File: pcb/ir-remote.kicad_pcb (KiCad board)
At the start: 2 copper layers, 127.9 x 53.5 mm, 104 parts, among them J1 Conn_01x02, J12 Conn_01x04, J2 Conn_01x02, J3 Pins_02x04_P2.54mm_SMT, J4 USB-C_Receptacle_Molex_217179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, J5 Jack_RCA_Stereo, J6 Conn_01x03, J7 Jack_RCA_Stereo, J8 Conn_01x02, U1 STM32G431CBTx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

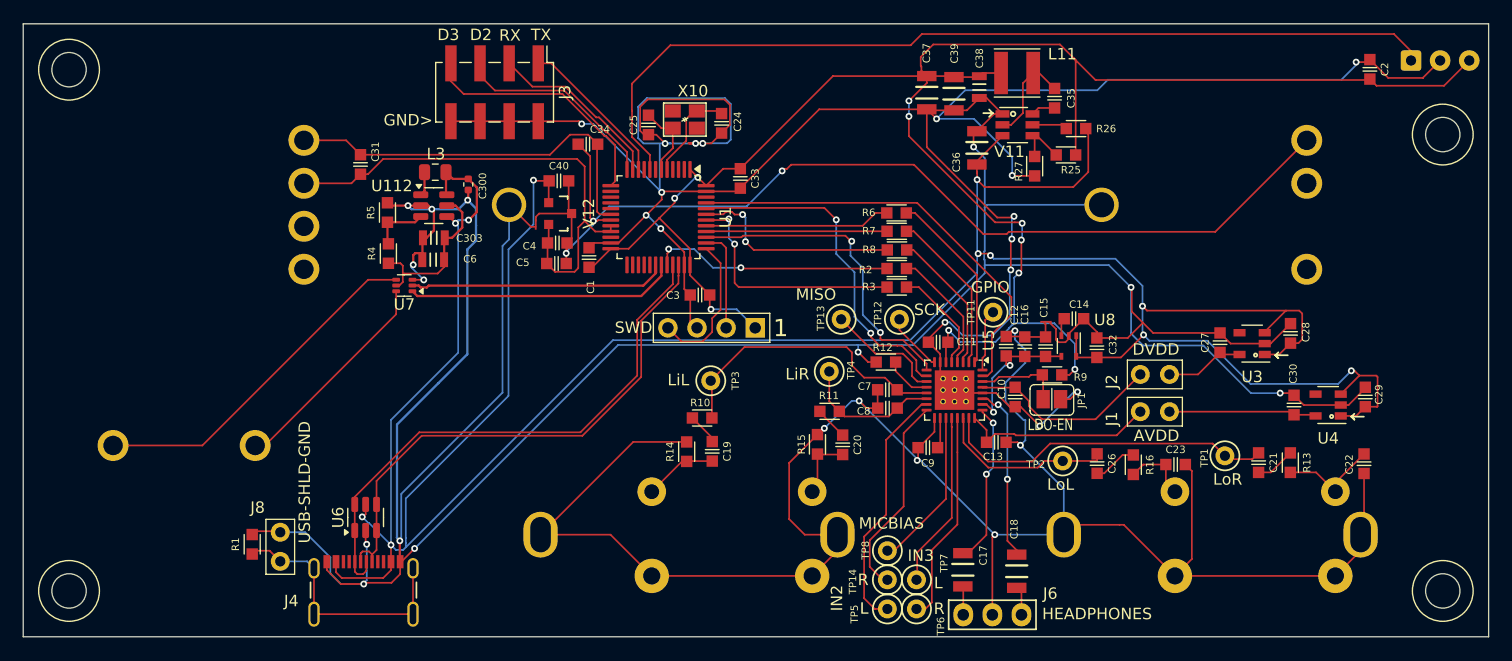
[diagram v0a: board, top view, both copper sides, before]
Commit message: Enclosure and PCB matched and fit
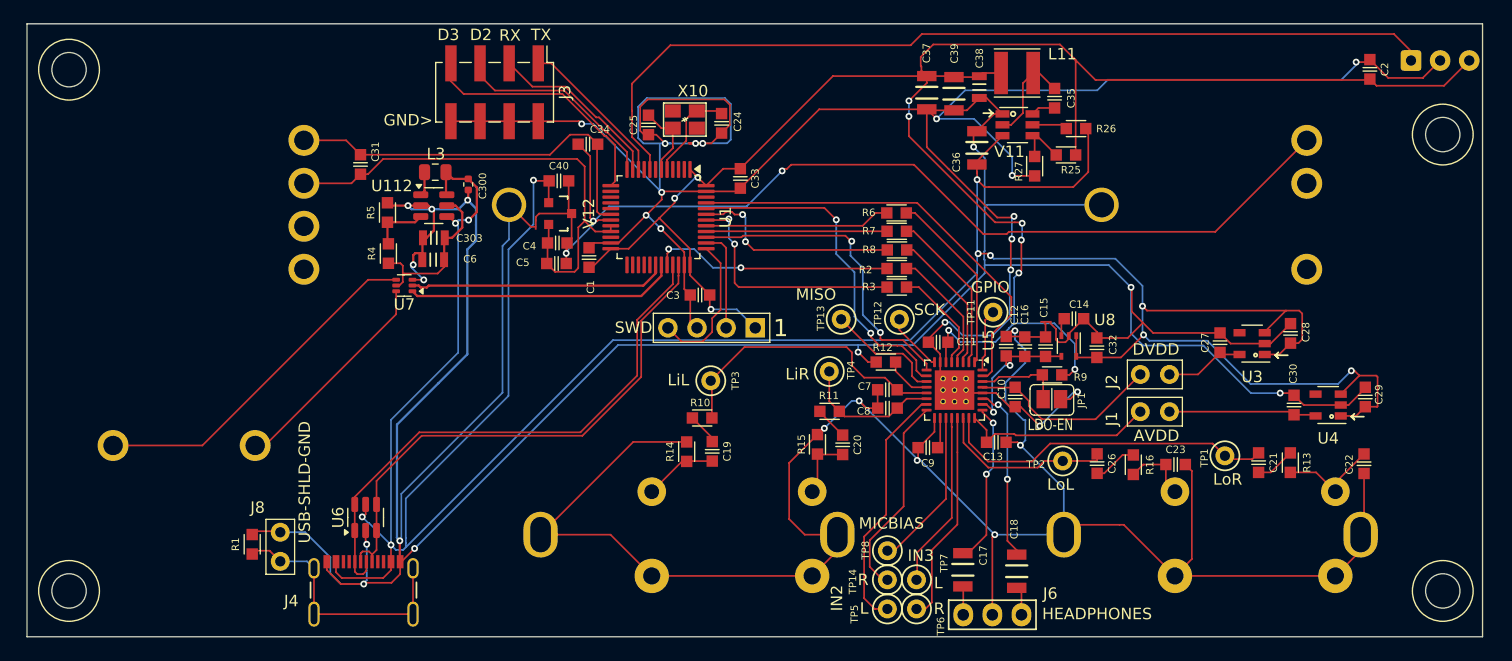
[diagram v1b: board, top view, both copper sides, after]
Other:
- board size 127.9 x 53.5 mm -> 127 x 53.5 mm
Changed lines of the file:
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@@
 		(embedded_fonts no)
 		(model "${KICAD6_3DMODEL_DIR}/Connector_PinHeader_2.54mm.3dshapes/PinHeader_2x04_P2.54mm_Vertical_SMD.wrl"
+			(hide yes)
 			(offset
 				(xyz 0 0 0)
@@
 		(embedded_fonts no)
 		(model "${KICAD6_3DMODEL_DIR}/Connector_PinHeader_2.54mm.3dshapes/PinHeader_1x02_P2.54mm_Vertical.wrl"
+			(hide yes)
 			(offset
 				(xyz 0 1.27 0)
@@
 		)
 		(model "${KICAD6_3DMODEL_DIR}/Connector_PinHeader_2.54mm.3dshapes/PinHeader_1x02_P2.54mm_Vertical.step"
+			(hide yes)
 			(offset
 				(xyz 0 1.27 0)
@@
 		)
 		(property "Value" "Conn_01x04"
-			(at 0.055 12.19 180)
+			(at 0.055 12.19 0)
 			(layer "F.SilkS")
 			(hide yes)
@@
 		(embedded_fonts no)
 		(model "${KICAD6_3DMODEL_DIR}/Connector_PinHeader_2.54mm.3dshapes/PinHeader_1x04_P2.54mm_Vertical.wrl"
+			(hide yes)
 			(offset
 				(xyz 0 3.81 0)
@@
 		(embedded_fonts no)
 		(model "${KICAD6_3DMODEL_DIR}/Connector_PinHeader_2.54mm.3dshapes/PinHeader_1x03_P2.54mm_Vertical.step"
+			(hide yes)
 			(offset
 				(xyz 0 2.54 0)
@@
 		(embedded_fonts no)
 		(model "${KICAD6_3DMODEL_DIR}/Connector_PinHeader_2.54mm.3dshapes/PinHeader_1x02_P2.54mm_Vertical.wrl"
+			(hide yes)
 			(offset
 				(xyz 0 1.27 0)
@@
 		)
 		(model "${KICAD6_3DMODEL_DIR}/Connector_PinHeader_2.54mm.3dshapes/PinHeader_1x02_P2.54mm_Vertical.step"
+			(hide yes)
 			(offset
 				(xyz 0 1.27 0)
@@
 		(embedded_fonts no)
 		(model "${KICAD6_3DMODEL_DIR}/Connector_PinHeader_2.54mm.3dshapes/PinHeader_1x02_P2.54mm_Vertical.wrl"
+			(hide yes)
 			(offset
 				(xyz 0 1.27 0)
@@
 		)
 		(model "${KICAD6_3DMODEL_DIR}/Connector_PinHeader_2.54mm.3dshapes/PinHeader_1x02_P2.54mm_Vertical.step"
+			(hide yes)
 			(offset
 				(xyz 0 1.27 0)
@@
 		)
 		(embedded_fonts no)
-		(model "${KICAD_4MS_LIBS}/3dmodels/Potentiometer.3dshapes/PSM60-082A.stp"
+		(model "${KICAD_4MS_LIBS}/3dmodels/Potentiometer.3dshapes/PSM60-081A-103B2.stp"
 			(offset
-				(xyz -58.3 46 144)
+				(xyz -4.25 -1.77 5.1)
 			)
 			(scale
@@
 		(model "${KICAD9_3DMODEL_DIR}/OptoDevice.3dshapes/Vishay_MINICAST-3Pin.step"
 			(offset
-				(xyz 0 0 0)
+				(xyz 0 0 7)
 			)
 			(scale
@@
 			)
 			(rotate
-				(xyz 0 0 0)
+				(xyz -0 -0 -0)
 			)
 		)
@@
 	)
 	(gr_line
-		(start 188.03 96.82)
-		(end 60.17 96.82)
+		(start 187.5 96.82)
+		(end 60.5 96.82)
 		(stroke
 			(width 0.05)
@@
 	)
 	(gr_line
-		(start 60.17 43.34)
-		(end 188.03 43.34)
+		(start 60.5 43.34)
+		(end 187.5 43.34)
 		(stroke
 			(width 0.05)
@@
 	)
 	(gr_line
-		(start 60.17 96.82)
-		(end 60.17 43.34)
+		(start 60.5 96.82)
+		(end 60.5 43.34)
 		(stroke
 			(width 0.05)
@@
 	)
 	(gr_line
-		(start 188.03 43.34)
-		(end 188.03 96.82)
+		(start 187.5 43.34)
+		(end 187.5 96.82)
 		(stroke
 			(width 0.05)
@@
 			(thickness 0.2)
 			(arrow_length 1.27)
-			(text_position_mode 0)
+			(text_position_mode 2)
 			(arrow_direction outward)
 			(extension_height 0.58642)
@@
 		)
 		(gr_text "94.17"
-			(at 136.945 108.92 0)
+			(at 136.51 114.9 0)
 			(layer "Dwgs.User")
 			(effects

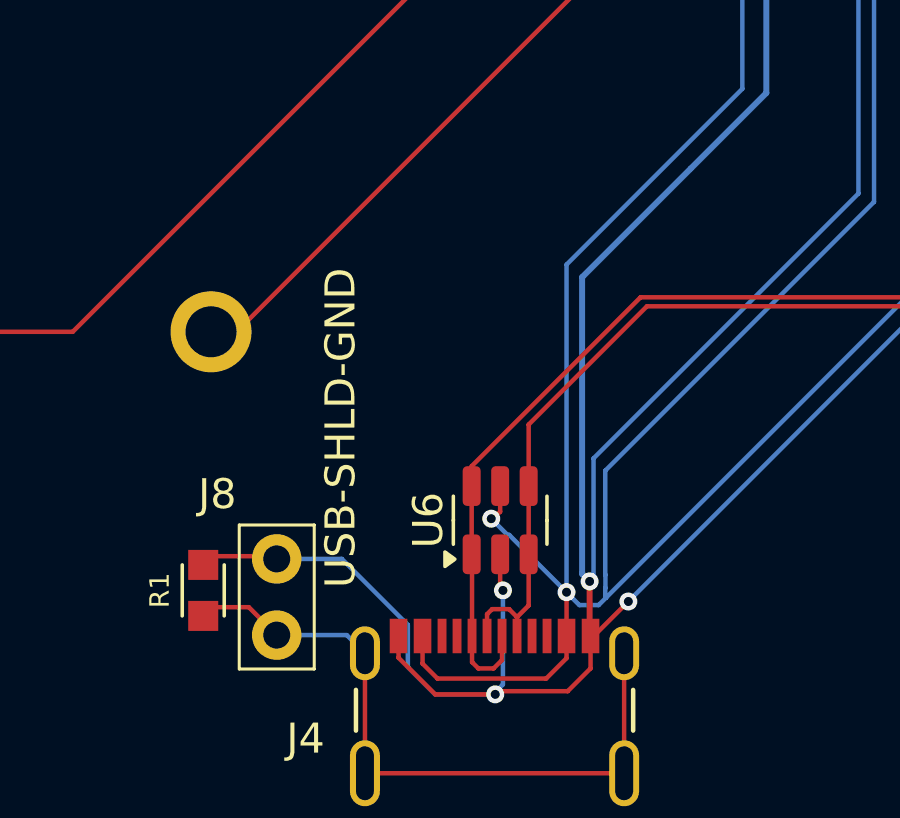
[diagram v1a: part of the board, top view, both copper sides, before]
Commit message: PCB: add missing 5.1k USB pull-downs
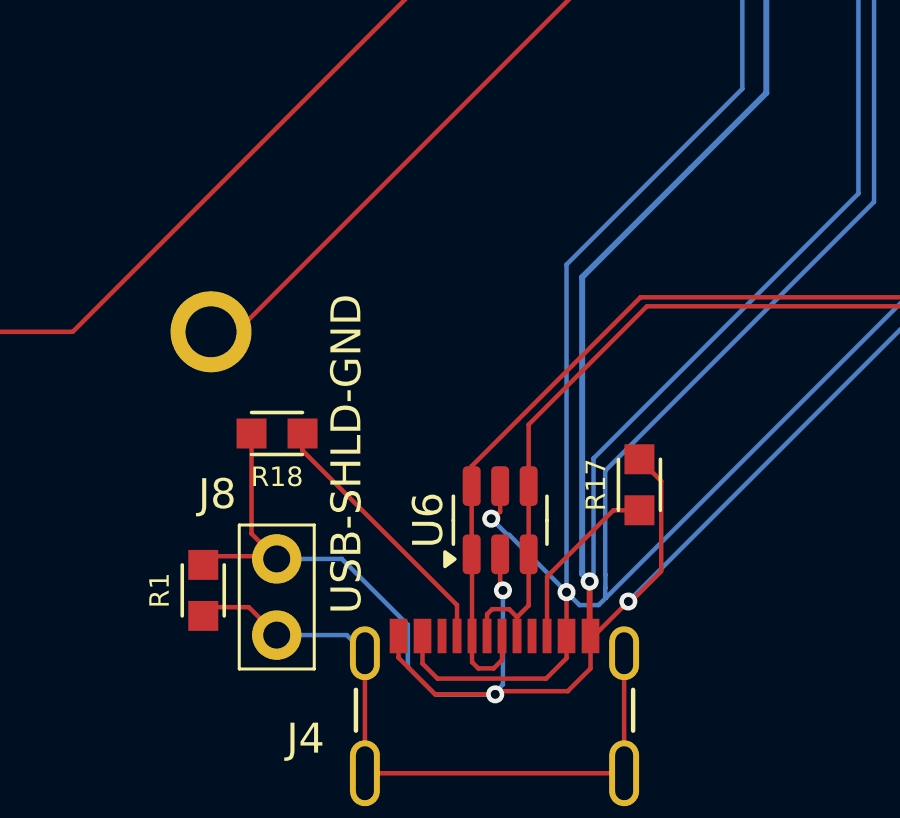
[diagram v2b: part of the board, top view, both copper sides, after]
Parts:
- added R17: 5.1k_0603, 4ms_Resistor:R_0603, F.Cu at (94.7, 85.2)
- added R18: 5.1k_0603, 4ms_Resistor:R_0603, F.Cu at (82.6, 83.5)
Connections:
- J4 pad A5: unconnected-(J4-CC1-PadA5) -> Net-(J4-CC1)
- J4 pad B5: unconnected-(J4-CC2-PadB5) -> Net-(J4-CC2)
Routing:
- net GND: track 513.7 -> 523.7 mm
- net Net-(J4-CC1): track 0.00 -> 8.88 mm
- net Net-(J4-CC2): track 0.00 -> 5.98 mm

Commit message: pcb: 20R=>33R, 2.2uF=>10uF. Change some JLC # to cheaper parts
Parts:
- C40: value 2.2uF_0603_25V -> 10uF_0603_10V
- R2, R3, R6, R7, R8: value 27Ω_0603 -> 33Ω_0603
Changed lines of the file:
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@@
 			)
 		)
-		(property "Value" "27Ω_0603"
+		(property "Value" "33Ω_0603"
 			(at 0 1.45 0)
 			(layer "F.Fab")
@@
 			)
 		)
-		(property "Description" "27Ω, 1%, 1/10W, 0603"
+		(property "Description" "33Ω, 1%, 1/10W, 0603"
 			(at 0 0 0)
 			(layer "F.Fab")
@@
 			)
 		)
-		(property "Specifications" "27Ω, 1%, 1/10W, 0603"
+		(property "Specifications" "33Ω, 1%, 1/10W, 0603"
 			(at 0 0 0)
 			(unlocked yes)
@@
 			)
 		)
-		(property "Part Number" "RC0603FR-0727RL"
+		(property "Part Number" "RC0603FR-0733RL"
 			(at 0 0 0)
 			(unlocked yes)
@@
 			)
 		)
-		(property "Display" "27Ω"
+		(property "Display" "33Ω"
 			(at 0 0 0)
 			(unlocked yes)
@@
 			)
 		)
-		(property "JLCPCB ID" "C137753"
+		(property "JLCPCB ID" "C23140"
 			(at 0 0 0)
 			(unlocked yes)
@@
 			)
 		)
-		(property "Value" "2.2uF_0603_25V"
+		(property "Value" "10uF_0603_10V"
 			(at 0.1 1.3 0)
 			(layer "F.Fab")
@@
 			)
 		)
-		(property "Description" ""
+		(property "Description" "10uF, Min. 10V X5R 10%"
 			(at 0 0 0)
 			(layer "F.Fab")
@@
 			)
 		)
-		(property "Specifications" "2.2uF, Min 25V 10% X5R"
+		(property "Specifications" "10uF, Min. 10V X5R 10%"
 			(at 0 0 0)
 			(unlocked yes)
@@
 			)
 		)
-		(property "Part Number" "GRM188R6YA225KA12D"
+		(property "Part Number" "GRM188R61A106KE69D"
 			(at 0 0 0)
 			(unlocked yes)
@@
 			)
 		)
-		(property "Display" "2.2uF"
+		(property "Display" "10uF/10V"
 			(at 0 0 0)
 			(unlocked yes)
@@
 			)
 		)
-		(property "JLCPCB ID" "C57895"
+		(property "JLCPCB ID" "C19702"
 			(at 0 0 0)
 			(unlocked yes)
@@
 			)
 		)
-		(property "Value" "27Ω_0603"
+		(property "Value" "33Ω_0603"
 			(at 0 1.45 0)
 			(layer "F.Fab")
@@
 			)
 		)
-		(property "Description" "27Ω, 1%, 1/10W, 0603"
+		(property "Description" "33Ω, 1%, 1/10W, 0603"
 			(at 0 0 0)
 			(layer "F.Fab")
@@
 			)
 		)
-		(property "Specifications" "27Ω, 1%, 1/10W, 0603"
+		(property "Specifications" "33Ω, 1%, 1/10W, 0603"
 			(at 0 0 0)
 			(unlocked yes)
@@
 			)
 		)
-		(property "Part Number" "RC0603FR-0727RL"
+		(property "Part Number" "RC0603FR-0733RL"
 			(at 0 0 0)
 			(unlocked yes)
@@
 			)
 		)
-		(property "Display" "27Ω"
+		(property "Display" "33Ω"
 			(at 0 0 0)
 			(unlocked yes)
@@
 			)
 		)
-		(property "JLCPCB ID" "C137753"
+		(property "JLCPCB ID" "C23140"
 			(at 0 0 0)
 			(unlocked yes)
@@
 			)
 		)
-		(property "Value" "27Ω_0603"
+		(property "Value" "33Ω_0603"
 			(at 0 1.45 0)
 			(layer "F.Fab")
@@
 			)
 		)
-		(property "Description" "27Ω, 1%, 1/10W, 0603"
+		(property "Description" "33Ω, 1%, 1/10W, 0603"
 			(at 0 0 0)
 			(layer "F.Fab")
@@
 			)
 		)
-		(property "Specifications" "27Ω, 1%, 1/10W, 0603"
+		(property "Specifications" "33Ω, 1%, 1/10W, 0603"
 			(at 0 0 0)
 			(unlocked yes)
@@
 			)
 		)
-		(property "Part Number" "RC0603FR-0727RL"
+		(property "Part Number" "RC0603FR-0733RL"
 			(at 0 0 0)
 			(unlocked yes)
@@
 			)
 		)
-		(property "Display" "27Ω"
+		(property "Display" "33Ω"
 			(at 0 0 0)
 			(unlocked yes)
@@
 			)
 		)
-		(property "JLCPCB ID" "C137753"
+		(property "JLCPCB ID" "C23140"
 			(at 0 0 0)
 			(unlocked yes)
@@
 			)
 		)
-		(property "Value" "27Ω_0603"
+		(property "Value" "33Ω_0603"
 			(at 0 1.45 0)
 			(layer "F.Fab")
@@
 			)
 		)
-		(property "Description" "27Ω, 1%, 1/10W, 0603"
+		(property "Description" "33Ω, 1%, 1/10W, 0603"
 			(at 0 0 0)
 			(layer "F.Fab")
@@
 			)
 		)
-		(property "Specifications" "27Ω, 1%, 1/10W, 0603"
+		(property "Specifications" "33Ω, 1%, 1/10W, 0603"
 			(at 0 0 0)
 			(unlocked yes)
@@
 			)
 		)
-		(property "Part Number" "RC0603FR-0727RL"
+		(property "Part Number" "RC0603FR-0733RL"
 			(at 0 0 0)
 			(unlocked yes)
@@
 			)
 		)
-		(property "Display" "27Ω"
+		(property "Display" "33Ω"
 			(at 0 0 0)
 			(unlocked yes)
@@
 			)
 		)
-		(property "JLCPCB ID" "C137753"
+		(property "JLCPCB ID" "C23140"
 			(at 0 0 0)
 			(unlocked yes)
@@
 			)
 		)
-		(property "Value" "27Ω_0603"
+		(property "Value" "33Ω_0603"
 			(at 0 1.45 0)
 			(layer "F.Fab")
@@
 			)
 		)
-		(property "Description" "27Ω, 1%, 1/10W, 0603"
+		(property "Description" "33Ω, 1%, 1/10W, 0603"
 			(at 0 0 0)
 			(layer "F.Fab")
@@
 			)
 		)
-		(property "Specifications" "27Ω, 1%, 1/10W, 0603"
+		(property "Specifications" "33Ω, 1%, 1/10W, 0603"
 			(at 0 0 0)
 			(unlocked yes)
@@
 			)
 		)
-		(property "Part Number" "RC0603FR-0727RL"
+		(property "Part Number" "RC0603FR-0733RL"
 			(at 0 0 0)
 			(unlocked yes)
@@
 			)
 		)
-		(property "Display" "27Ω"
+		(property "Display" "33Ω"
 			(at 0 0 0)
 			(unlocked yes)
@@
 			)
 		)
-		(property "JLCPCB ID" "C137753"
+		(property "JLCPCB ID" "C23140"
 			(at 0 0 0)
 			(unlocked yes)
